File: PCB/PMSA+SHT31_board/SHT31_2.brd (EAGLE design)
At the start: 41.7 x 49.2 mm, 8 parts, among them CN2 CON_PINHD-2X15, U2 SHT31-DIS

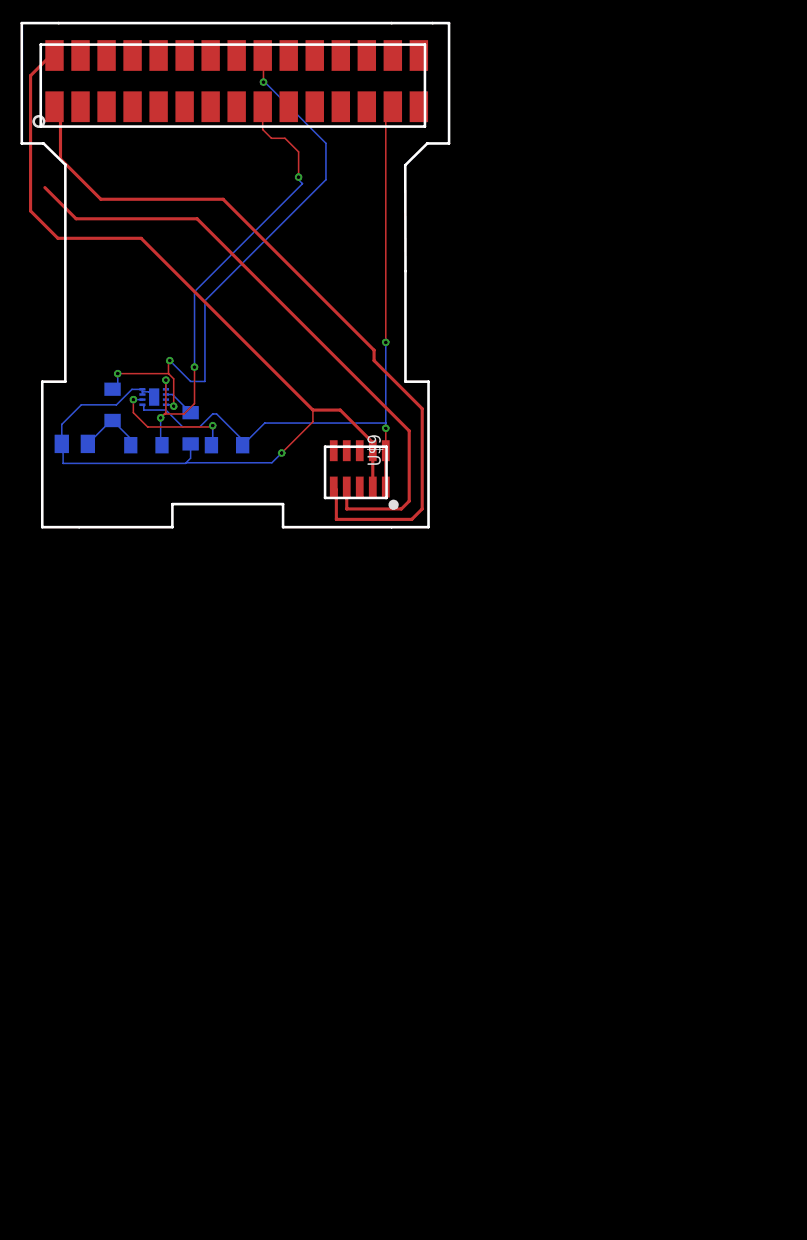
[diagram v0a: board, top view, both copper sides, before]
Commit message: insertion NOX & CO Captor
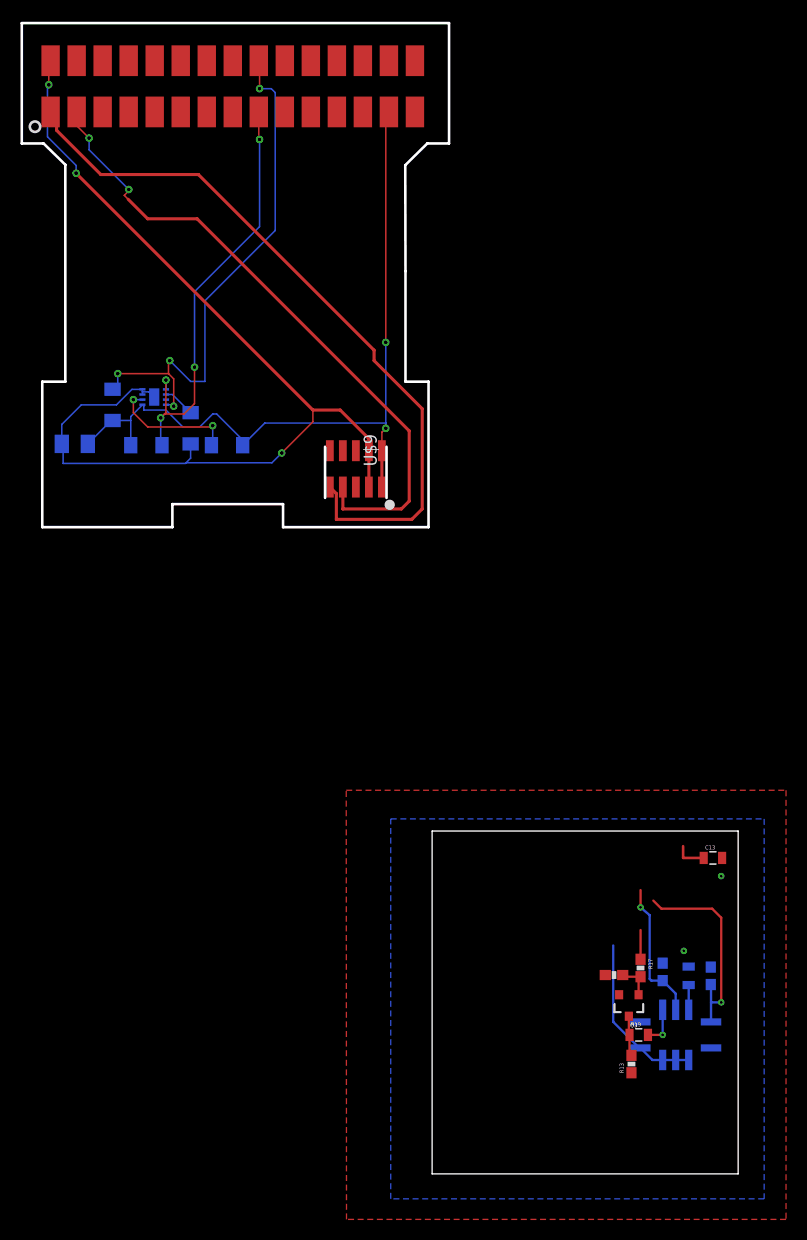
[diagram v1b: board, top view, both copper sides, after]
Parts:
- added C13: 10uF, SparkFun-Capacitors:0805
- added Q3: MOSFET-NCHANNELBSS138, SparkFun-DiscreteSemi:SOT23-3
- added R13: 51, SparkFun-Resistors:0603-RES
- added R17: 100, SparkFun-Resistors:0603-RES
- added R18: 100k, SparkFun-Resistors:0603-RES
- added R19, R21: 82, SparkFun-Resistors:0805
- added R20: 22K, SparkFun-Resistors:0603-RES
- added R22: 47K, SparkFun-Resistors:0603-RES
- added U3: MICS-4514, SparkFun-Sensors:MICS_10-SMD
- moved CN2 0.64 mm to (18.6, 43.0)
- moved U$9 0.38 mm to (30.6, 5.69)
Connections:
- new net N$13: Q3.1, R17.2, R18.2
- new net N$15: R19.2, U3.A
- new net N$16: R21.2, U3.C
- new net N$7: Q3.3, R13.2, R19.1
- new net VNOX: CN2.P$19, R20.2, U3.B
- new net VRED: CN2.P$20, R22.2, U3.D
- net GND: now also C13.2, Q3.2, R13.1, R18.1, R20.1, R21.1, R22.1
- net PT_TX: now also R17.1
- net VDD: now also C13.1, U3.F, U3.G, U3.H, U3.J
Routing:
- net VDD: track 71.8 -> 94.7 mm
- net VRED: track 0.00 -> 20.2 mm, vias 0 -> 1
- net VNOX: track 0.00 -> 13.8 mm, vias 0 -> 1
- net GND: track 107.9 -> 101.2 mm, vias 1 -> 5
- net SDA: track 47.1 -> 42.7 mm
- net N$7: track 0.00 -> 3.92 mm
- net N$15: track 0.00 -> 3.89 mm, vias 0 -> 1
- net SCL: track 55.8 -> 52.0 mm
- net N$13: track 0.00 -> 3.65 mm
- net PT_RX: track 60.8 -> 63.6 mm, vias 0 -> 2
- net N$16: track 0.00 -> 2.42 mm
- net PT_TX: track 73.2 -> 74.4 mm
- added copper zone on layer 1, net GND
- added copper zone on layer 16, net GND
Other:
- board size 41.7 x 49.2 mm -> 69.9 x 112.3 mm

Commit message: insertion NOX & CO Captor
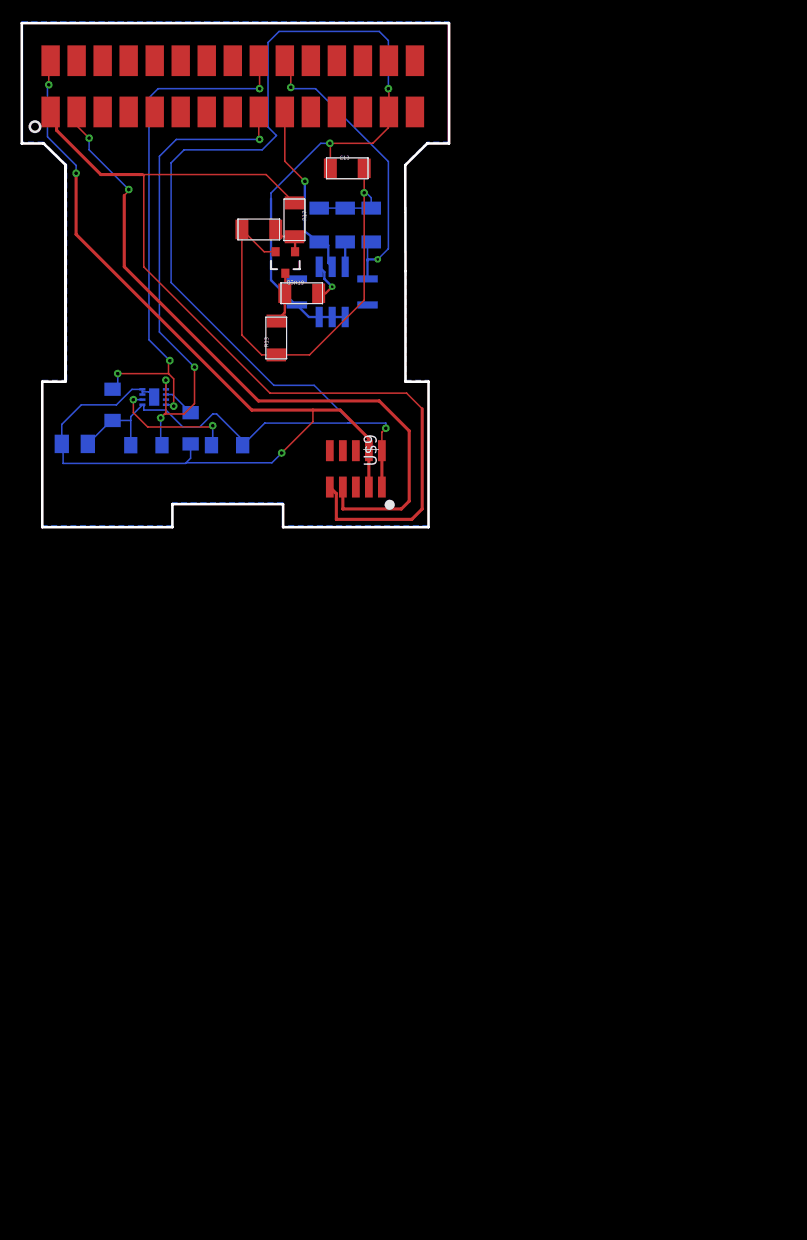
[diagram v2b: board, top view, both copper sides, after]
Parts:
- C13: device SparkFun-Capacitors:0805 -> fab:R1206FAB
- R13, R17, R20, R22: device SparkFun-Resistors:0603-RES -> fab:R1206FAB
- R18: value 100k -> 100K; device SparkFun-Resistors:0603-RES -> fab:R1206FAB
- R19, R21: device SparkFun-Resistors:0805 -> fab:R1206FAB
- moved R18 80.6 mm to (21.1, 29.1)
- moved R21 80.6 mm to (29.6, 29.5)
- moved R17 80.5 mm to (24.6, 30.0)
- moved R22 80.4 mm to (32.1, 29.5)
- moved R20 80.2 mm to (27.0, 29.5)
- moved Q3 79.9 mm to (23.7, 25.9)
- moved U3 79.9 mm to (28.3, 23.0)
- moved R19 79.5 mm to (25.3, 22.8)
- moved R13 78.9 mm to (22.8, 18.5)
- moved C13 76.2 mm to (29.8, 35.0)
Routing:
- net VDD: track 94.7 -> 155.6 mm, vias 2 -> 3
- net GND: track 101.2 -> 154.0 mm, vias 5 -> 4
- net PT_TX: track 74.4 -> 92.4 mm
- net VRED: track 20.2 -> 30.2 mm, vias 1 -> 2
- net SDA: track 42.7 -> 50.3 mm
- net PT_RX: track 63.6 -> 67.7 mm
- net VNOX: track 13.8 -> 17.4 mm
- net N$7: track 3.92 -> 5.06 mm
- net SCL: track 52.0 -> 52.6 mm
- removed copper zone on layer 1, net GND
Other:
- board size 69.9 x 112.3 mm -> 41.7 x 49.2 mm

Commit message: pcbV2 ready to go!
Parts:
- moved R18 0.63 mm to (20.6, 28.7)
- moved R17 0.40 mm to (24.5, 30.4)
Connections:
- new net PRE26: CN2.P$26, R17.1
- net PT_TX: no longer R17.1
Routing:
- net PRE26: track 0.00 -> 18.2 mm
- net PT_TX: track 92.4 -> 76.5 mm
- net N$13: track 3.98 -> 5.29 mm
- net GND: track 154.0 -> 154.2 mm, vias 4 -> 19
- added copper zone on layer 1, net GND

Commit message: 3DPACKAGE!
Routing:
- net GND: track 154.2 -> 347.2 mm
